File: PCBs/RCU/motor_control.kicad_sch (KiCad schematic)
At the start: 14 parts

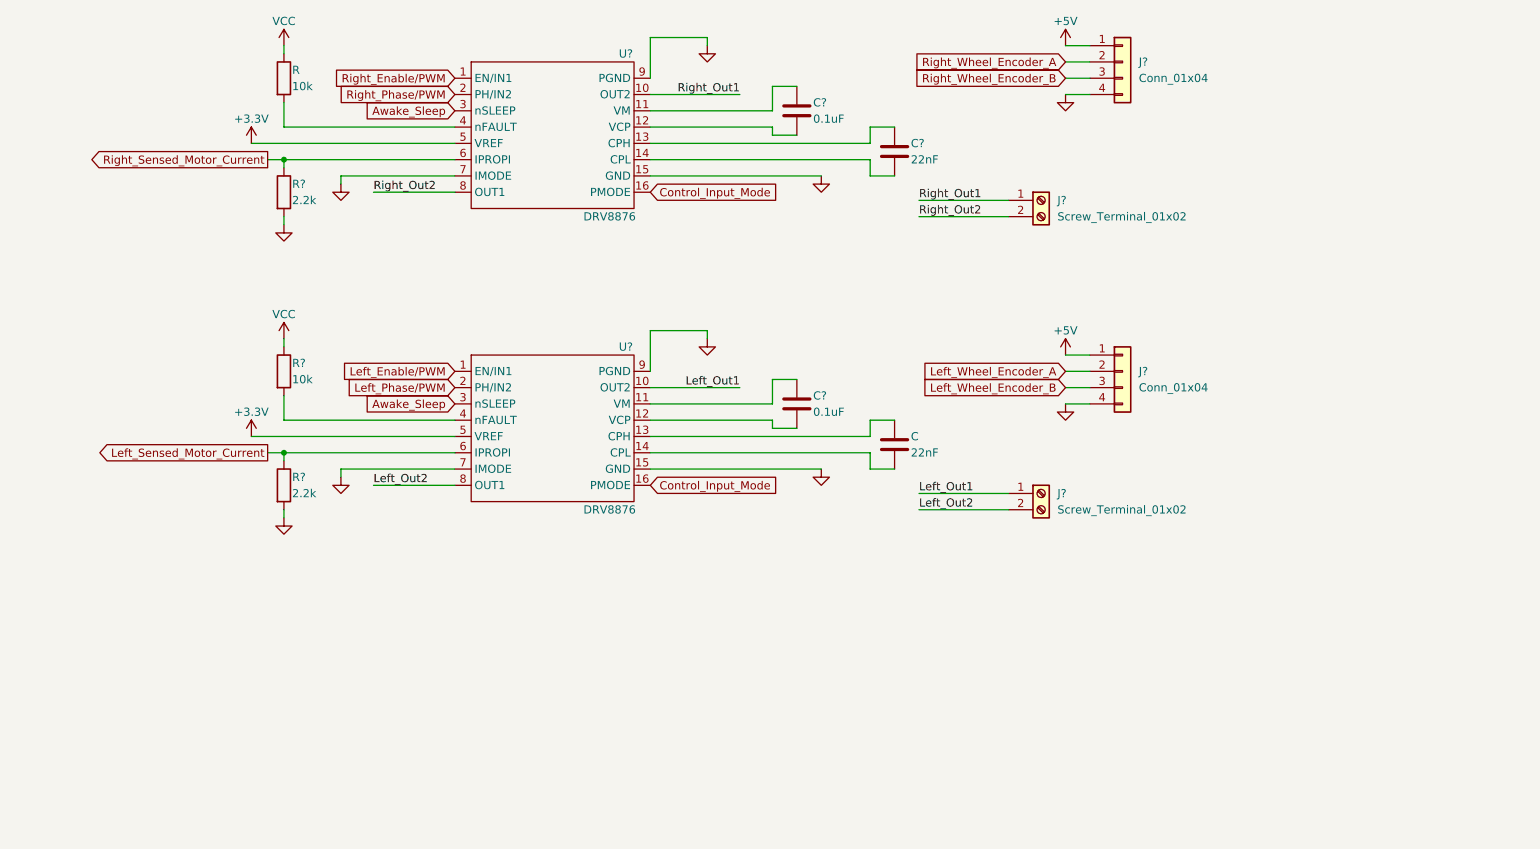
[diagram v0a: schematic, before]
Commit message: Add output buffer to IPROPI pin of Motor Driver ICs and low pass RC filter and input buffer to ADCs
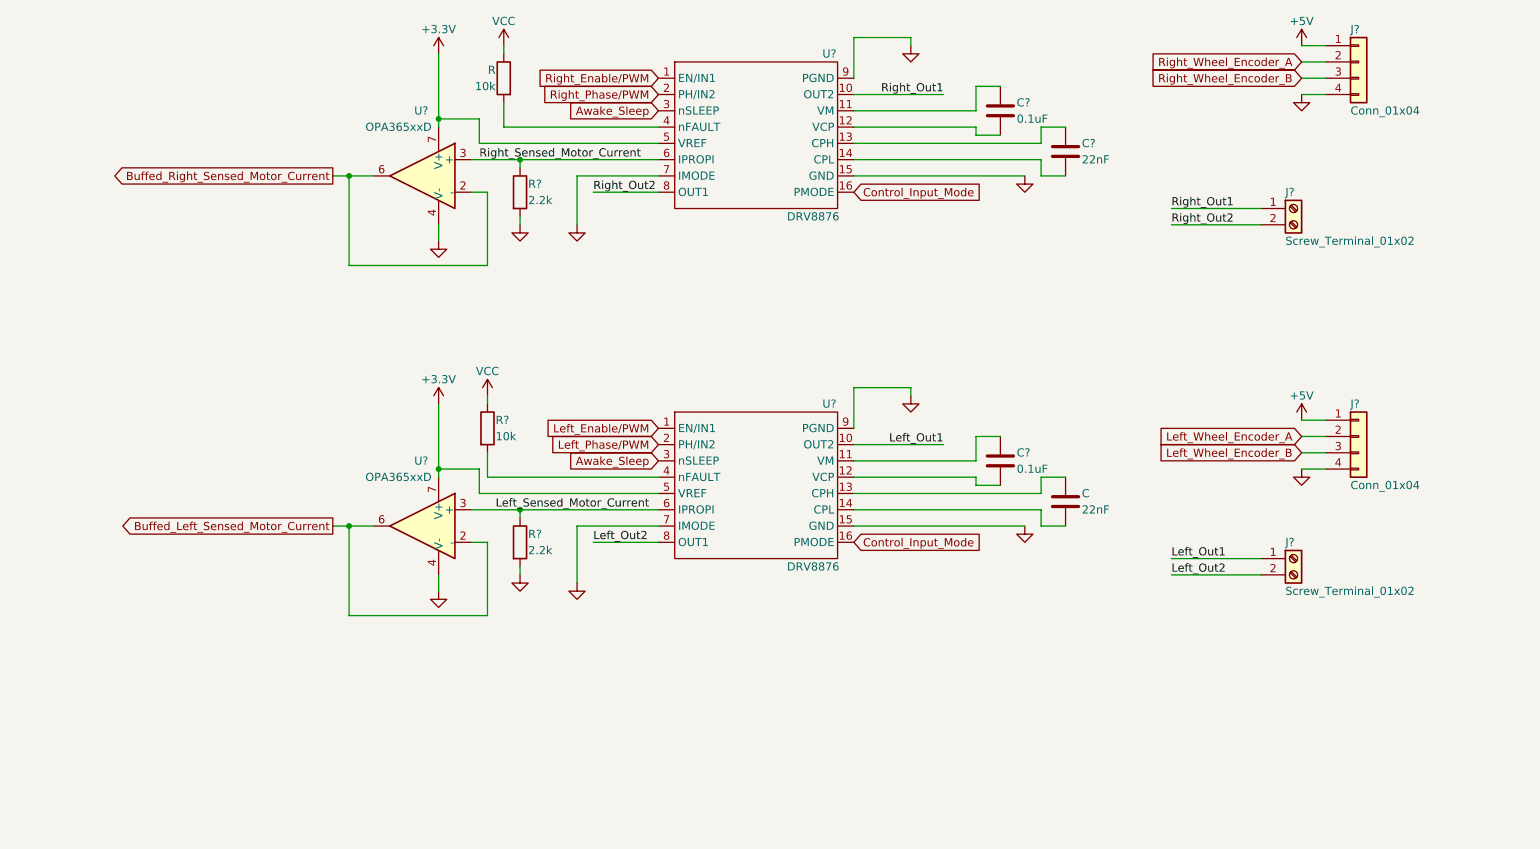
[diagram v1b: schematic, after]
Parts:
- added U? (x2): OPA365xxD, Package_SO:SOIC-8_3.9x4.9mm_P1.27mm, symbol Amplifier_Operational:OPA365xxD
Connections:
- net +3V3: now also U?.7 (V+), U?.7 (V+)
- net GND: now also U?.4 (V-), U?.4 (V-)
- net Left_Sensed_Motor_Current: now also U?.3 (+)
- net Right_Sensed_Motor_Current: now also U?.3 (+)
- new net Buffed_Left_Sensed_Motor_Current: U?.2 (-), U?.6
- new net Buffed_Right_Sensed_Motor_Current: U?.2 (-), U?.6
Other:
- moved on the sheet: C, C?, J?, R, R?, U?

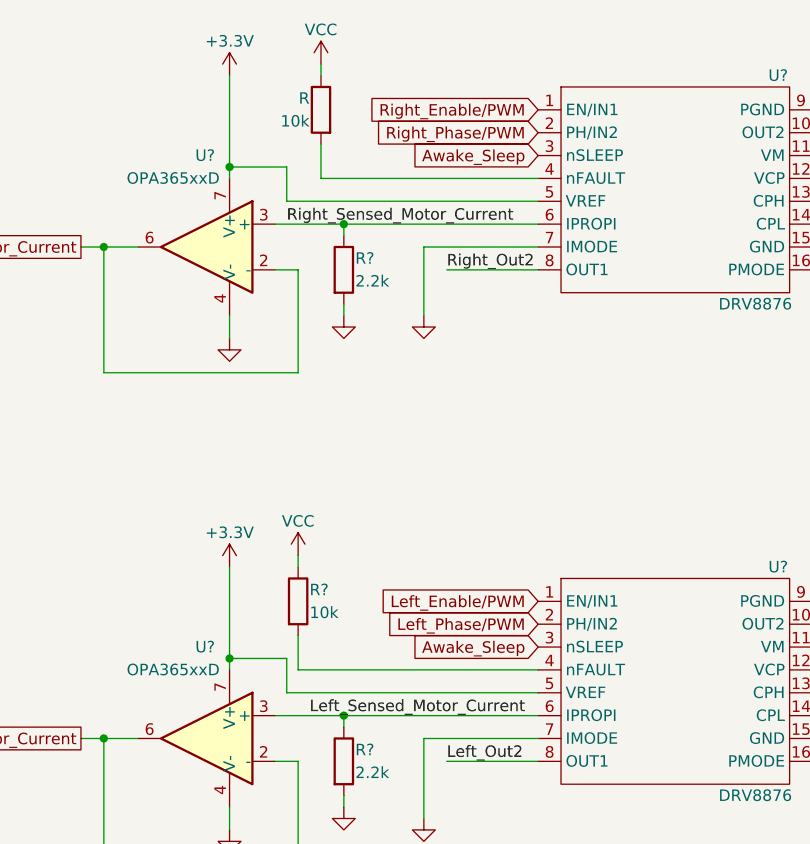
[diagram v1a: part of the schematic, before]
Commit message: Microcontroller will take nFaults of both motor controllers as inputs
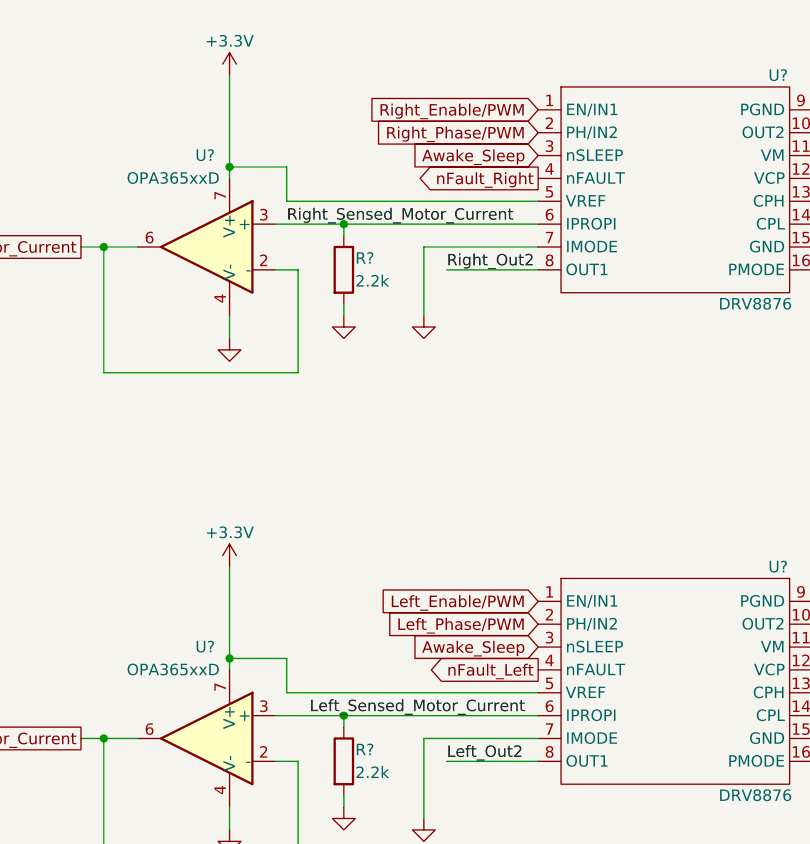
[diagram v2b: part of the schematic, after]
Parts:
- removed R, R?: 10k, symbol Device:R
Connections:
- net nFault_Right: now reaches U?.4 (nFAULT)
- net nFault_Left: now reaches U?.4 (nFAULT)
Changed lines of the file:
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@@
-    (stroke (width 0) (type default) (color 0 0 0 0))
-  )
-  (wire (pts (xy 82.55 31.75) (xy 82.55 35.56))
     (stroke (width 0) (type default) (color 0 0 0 0))
   )
@@
     (stroke (width 0) (type default) (color 0 0 0 0))
   )
-  (wire (pts (xy 80.01 86.36) (xy 80.01 90.17))
-    (stroke (width 0) (type default) (color 0 0 0 0))
-  )
   (wire (pts (xy 166.37 90.17) (xy 170.18 90.17))
     (stroke (width 0) (type default) (color 0 0 0 0))
@@
     (stroke (width 0) (type default) (color 0 0 0 0))
   )
-  (wire (pts (xy 80.01 77.47) (xy 80.01 78.74))
-    (stroke (width 0) (type default) (color 0 0 0 0))
-  )
-  (wire (pts (xy 82.55 22.86) (xy 82.55 24.13))
-    (stroke (width 0) (type default) (color 0 0 0 0))
-  )
   (wire (pts (xy 137.16 27.94) (xy 137.16 21.59))
     (stroke (width 0) (type default) (color 0 0 0 0))
@@
     (stroke (width 0) (type default) (color 0 0 0 0))
   )
-  (wire (pts (xy 82.55 35.56) (xy 106.68 35.56))
-    (stroke (width 0) (type default) (color 0 0 0 0))
-  )
   (wire (pts (xy 58.42 57.15) (xy 58.42 43.18))
     (stroke (width 0) (type default) (color 0 0 0 0))
@@
   )
   (wire (pts (xy 166.37 35.56) (xy 170.18 35.56))
-    (stroke (width 0) (type default) (color 0 0 0 0))
-  )
-  (wire (pts (xy 80.01 90.17) (xy 106.68 90.17))
     (stroke (width 0) (type default) (color 0 0 0 0))
   )
@@
     (effects (font (size 1.27 1.27)) (justify right))
     (property "Intersheet References" "${INTERSHEET_REFS}" (id 0) (at 183.8536 86.2806 0)
+      (effects (font (size 1.27 1.27)) (justify right) hide)
+    )
+  )
+  (global_label "nFault_Left" (shape output) (at 106.68 90.17 180) (fields_autoplaced)
+    (effects (font (size 1.27 1.27)) (justify right))
+    (property "Intersheet References" "${INTERSHEET_REFS}" (id 0) (at 93.8045 90.0906 0)
       (effects (font (size 1.27 1.27)) (justify right) hide)
     )
@@
     (effects (font (size 1.27 1.27)) (justify right))
     (property "Intersheet References" "${INTERSHEET_REFS}" (id 0) (at 87.8779 82.4706 0)
+      (effects (font (size 1.27 1.27)) (justify right) hide)
+    )
+  )
+  (global_label "nFault_Right" (shape output) (at 106.68 35.56 180) (fields_autoplaced)
+    (effects (font (size 1.27 1.27)) (justify right))
+    (property "Intersheet References" "${INTERSHEET_REFS}" (id 0) (at 92.474 35.4806 0)
       (effects (font (size 1.27 1.27)) (justify right) hide)
     )
@@
     (pin "1")
   )
-  (symbol (lib_id "power:VCC") (at 82.55 22.86 0) (unit 1)
-    (in_bom yes) (on_board yes)
-    (property "Reference" "#PWR?" (id 0) (at 82.55 26.67 0)
-      (effects (font (size 1.27 1.27)) hide)
-    )
-    (property "Value" "VCC" (id 1) (at 82.55 19.05 0))
-    (property "Footprint" "" (id 2) (at 82.55 22.86 0)
-      (effects (font (size 1.27 1.27)) hide)
-    )
-    (property "Datasheet" "" (id 3) (at 82.55 22.86 0)
-      (effects (font (size 1.27 1.27)) hide)
-    )
-    (pin "1")
-  )
   (symbol (lib_id "power:GND") (at 72.39 53.34 0) (unit 1)
     (in_bom yes) (on_board yes) (fields_autoplaced)
@@
     (pin "1")
   )
-  (symbol (lib_id "power:VCC") (at 80.01 77.47 0) (unit 1)
-    (in_bom yes) (on_board yes)
-    (property "Reference" "#PWR?" (id 0) (at 80.01 81.28 0)
-      (effects (font (size 1.27 1.27)) hide)
-    )
-    (property "Value" "VCC" (id 1) (at 80.01 73.66 0))
-    (property "Footprint" "" (id 2) (at 80.01 77.47 0)
-      (effects (font (size 1.27 1.27)) hide)
-    )
-    (property "Datasheet" "" (id 3) (at 80.01 77.47 0)
-      (effects (font (size 1.27 1.27)) hide)
-    )
-    (pin "1")
-  )
   (symbol (lib_id "Connector:Screw_Terminal_01x02") (at 205.74 48.26 0) (unit 1)
     (in_bom yes) (on_board yes)
@@
     )
     (pin "1")
-  )
-  (symbol (lib_id "Device:R") (at 80.01 82.55 0) (unit 1)
-    (in_bom yes) (on_board yes)
-    (property "Reference" "R?" (id 0) (at 81.28 81.28 0)
-      (effects (font (size 1.27 1.27)) (justify left))
-    )
-    (property "Value" "10k" (id 1) (at 81.28 83.82 0)
-      (effects (font (size 1.27 1.27)) (justify left))
-    )
-    (property "Footprint" "" (id 2) (at 78.232 82.55 90)
-      (effects (font (size 1.27 1.27)) hide)
-    )
-    (property "Datasheet" "~" (id 3) (at 80.01 82.55 0)
-      (effects (font (size 1.27 1.27)) hide)
-    )
-    (pin "1")
-    (pin "2")
   )
   (symbol (lib_id "Connector_Generic:Conn_01x04") (at 215.9 25.4 0) (unit 1)
@@
     (pin "1")
   )
-  (symbol (lib_id "Device:R") (at 82.55 27.94 0) (mirror y) (unit 1)
-    (in_bom yes) (on_board yes)
-    (property "Reference" "R" (id 0) (at 81.28 26.67 0)
-      (effects (font (size 1.27 1.27)) (justify left))
-    )
-    (property "Value" "10k" (id 1) (at 81.28 29.21 0)
-      (effects (font (size 1.27 1.27)) (justify left))
-    )
-    (property "Footprint" "" (id 2) (at 84.328 27.94 90)
-      (effects (font (size 1.27 1.27)) hide)
-    )
-    (property "Datasheet" "~" (id 3) (at 82.55 27.94 0)
-      (effects (font (size 1.27 1.27)) hide)
-    )
-    (pin "1")
-    (pin "2")
-  )
   (symbol (lib_id "power:GND") (at 163.83 97.79 0) (unit 1)

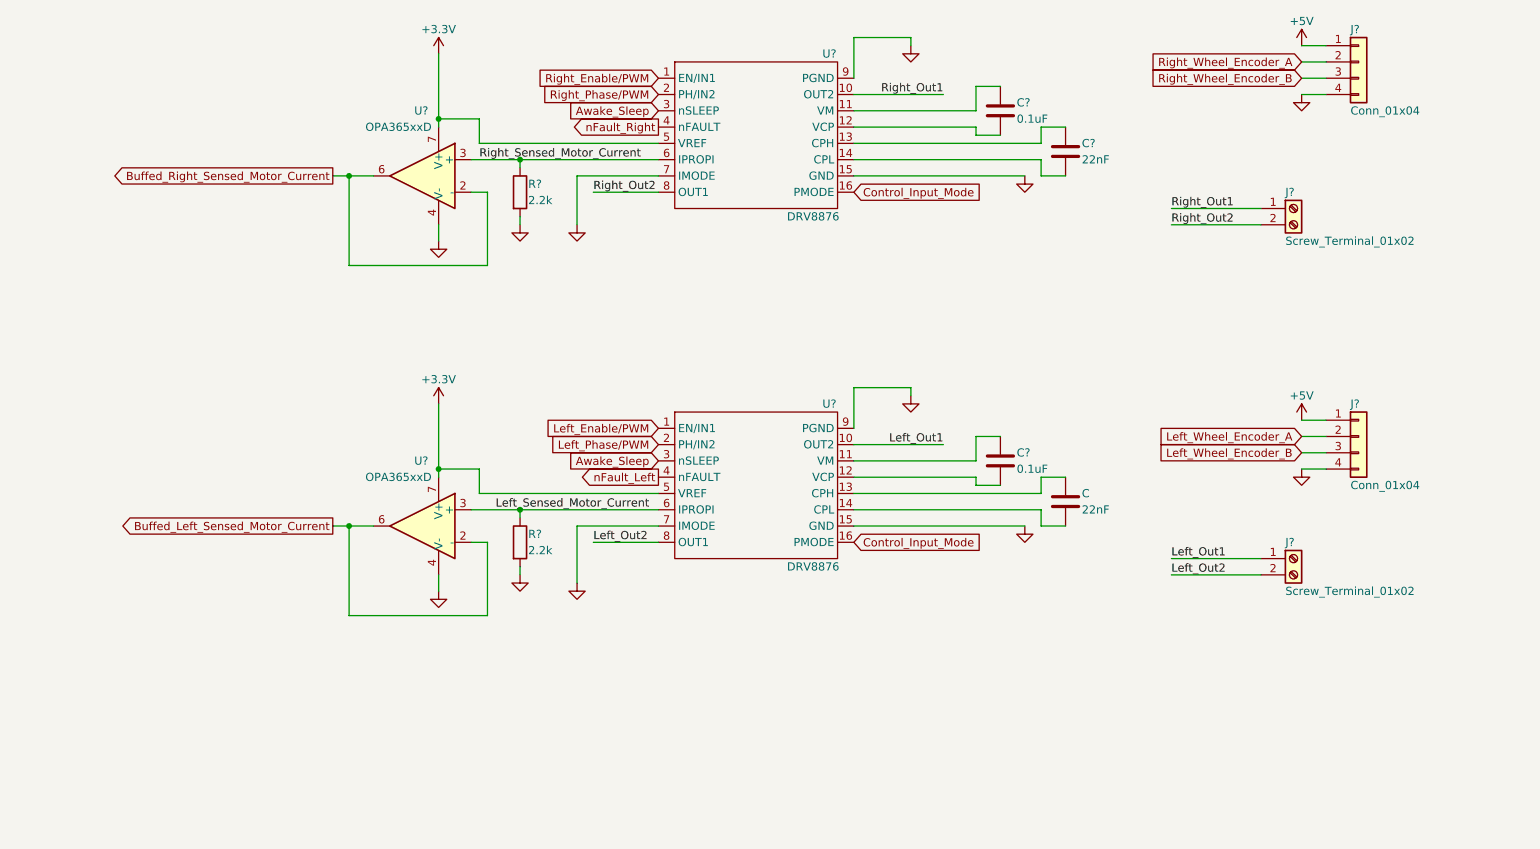
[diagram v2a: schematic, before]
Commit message: Add USB power filter circuitry and corrected Motor Driver schematic
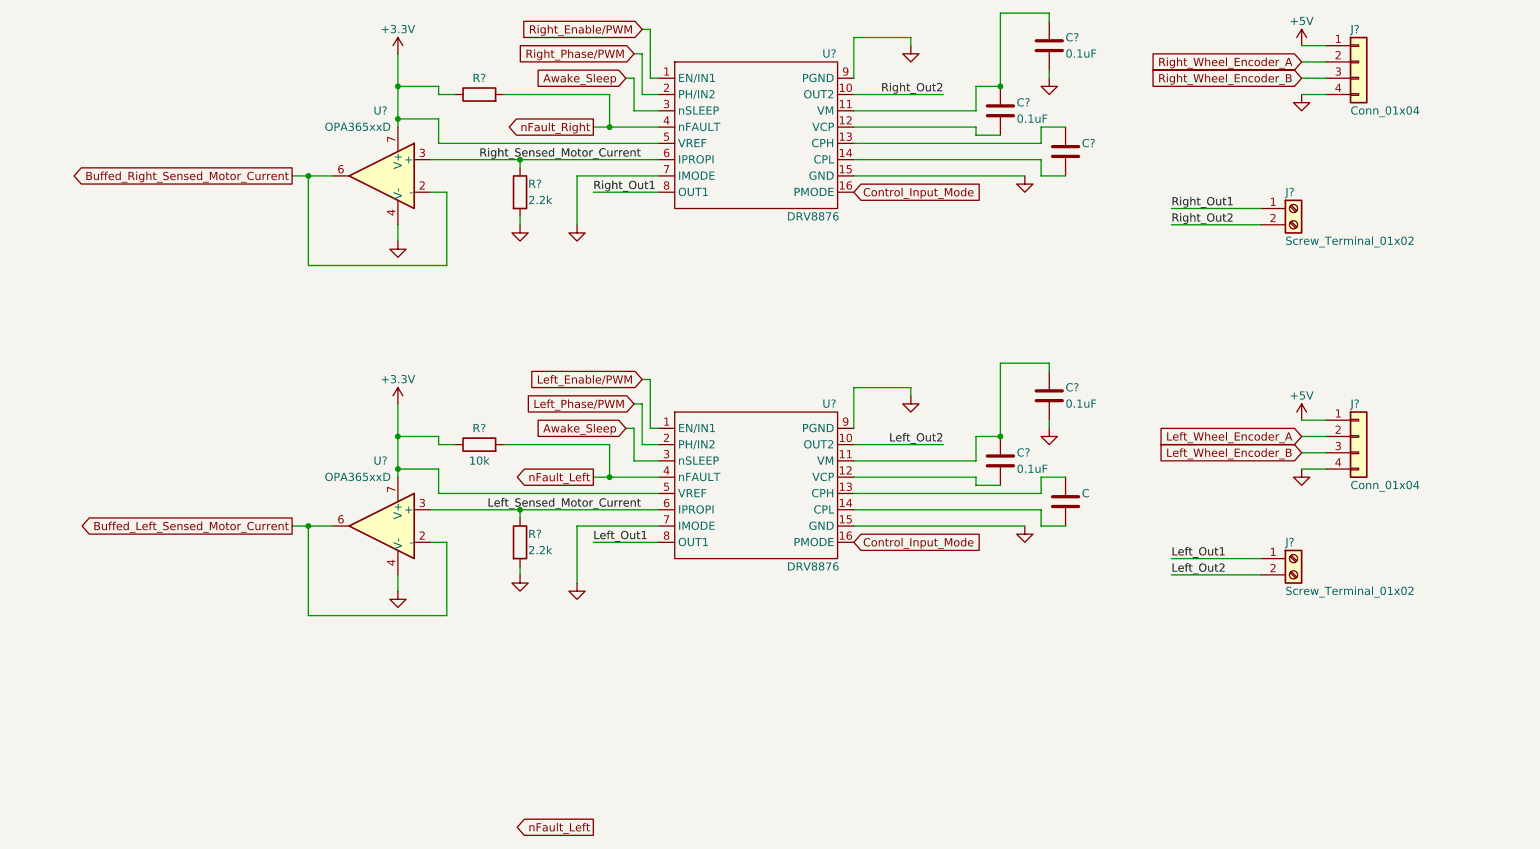
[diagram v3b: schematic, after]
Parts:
- added C? (x2): 0.1uF, symbol Device:C
- added R?: (no value), symbol Device:R
- added R?: 10k, symbol Device:R
- C, C?: value 22nF -> (none)
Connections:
- net +3V3: now also R?.1, R?.1
- net GND: now also C?.2, C?.2
- net Left_Out1: now also U?.8 (OUT1); no longer U?.10 (OUT2)
- net Left_Out2: now also U?.10 (OUT2); no longer U?.8 (OUT1)
- net Right_Out1: now also U?.8 (OUT1); no longer U?.10 (OUT2)
- net Right_Out2: now also U?.10 (OUT2); no longer U?.8 (OUT1)
- net nFault_Left: now also R?.2
- net nFault_Right: now also R?.2
- net at C?.1, U?.11 (VM): now also C?.1 (x2)
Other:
- moved on the sheet: U?
